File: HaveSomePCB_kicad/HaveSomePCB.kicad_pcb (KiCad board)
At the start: 2 copper layers, 7.6 x 18.4 mm, 15 parts

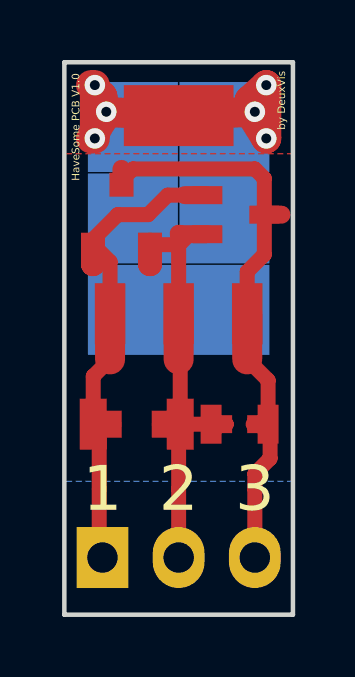
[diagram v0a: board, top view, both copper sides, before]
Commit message: Version 1.1 :  - Trying to let PCBs.io manufacturing process actually produce vias by not burying them under a pad.  - Beefier traces, especially on center pin - thanks to original Awsome PCB designer Simon for the suggestion on hackaday.io.  - Beefier vias for better current/heat transfer.  - Linked pad 2 and 4 of SOT223 for footprint compatible packages which lack the 2nd pin like DPAK, D²PAK...  - Added silkscreen annotations of pads to pins id matching - thanks to warhawk-avg on hackaday.io for the suggestion.
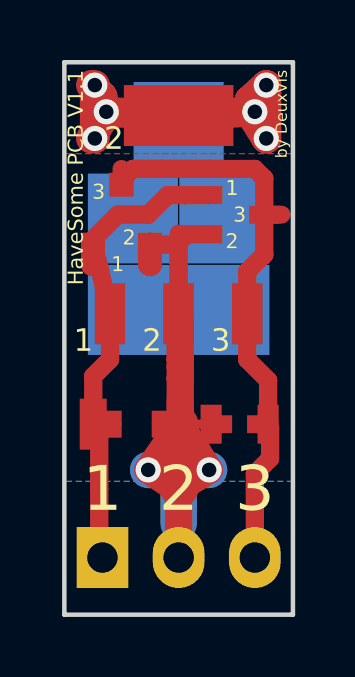
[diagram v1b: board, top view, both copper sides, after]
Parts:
- removed the REF**22 at (141.2, 96.1)
- moved REF**22 1.52 mm to (139.7, 96.1)
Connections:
- REF**12 pad 1: Net-(PINS1-Pad4) -> Net-(PINS1-Pad2)
- REF**13 pad 1: Net-(PINS1-Pad4) -> Net-(PINS1-Pad2)
- REF**22 pad 1: Net-(PINS1-Pad4) -> Net-(PINS1-Pad2) (x2)
- REF**23 pad 1: Net-(PINS1-Pad4) -> Net-(PINS1-Pad2)
- SOT223 pad 4: Net-(PINS1-Pad4) -> Net-(PINS1-Pad2)
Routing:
- net Net-(PINS1-Pad2): track 18.9 -> 49.0 mm, vias 0 -> 8
- net Net-(PINS1-Pad4): track 12.7 -> 0.00 mm, vias 6 -> 0
- added copper zone on B.Cu, net Net-(PINS1-Pad2)
- added copper zone on F.Cu, net Net-(PINS1-Pad2)
- removed copper zone on B.Cu, net Net-(PINS1-Pad4)
- removed copper zone on F.Cu, net Net-(PINS1-Pad4)
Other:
- net class Beefier added: clearance 0.1524, trace_width 0.2286, via_dia 0.8382, via_drill 0.4826
- net class Gross added: clearance 0.1524, trace_width 0.3048, via_dia 0.9906, via_drill 0.635
- board text added: "HaveSome PCB V1.1"
- board text removed: "HaveSome PCB V1.0"
